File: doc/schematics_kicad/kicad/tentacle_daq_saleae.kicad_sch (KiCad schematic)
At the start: 5 parts, among them T901 tentacle, T902 tentacle, T903 tentacle

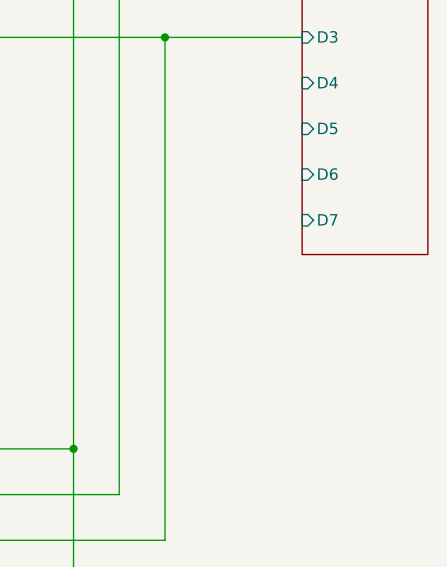
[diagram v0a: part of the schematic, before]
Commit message: MCU names as in micropython-git
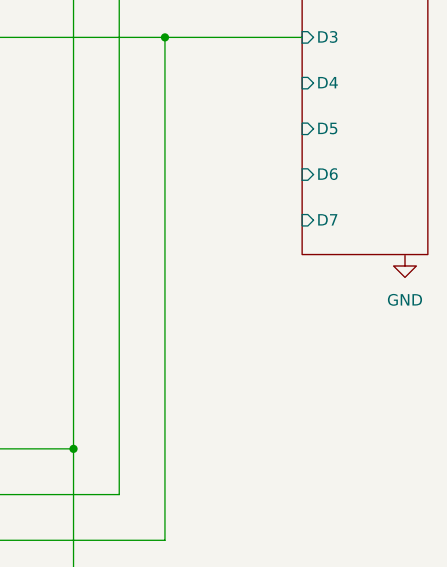
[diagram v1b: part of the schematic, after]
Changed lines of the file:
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@@
+	)
+	(symbol
+		(lib_id "power:GND")
+		(at 194.31 100.33 0)
+		(unit 1)
+		(exclude_from_sim no)
+		(in_bom yes)
+		(on_board yes)
+		(dnp no)
+		(fields_autoplaced yes)
+		(property "Reference" "#PWR0503"
+			(at 194.31 106.68 0)
+			(effects
+				(font
+					(size 1.27 1.27)
+				)
+				(hide yes)
+			)
+		)
+		(property "Value" "GND"
+			(at 194.31 105.41 0)
+			(effects
+				(font
+					(size 1.27 1.27)
+				)
+			)
+		)
+		(property "Footprint" ""
+			(at 194.31 100.33 0)
+			(effects
+				(font
+					(size 1.27 1.27)
+				)
+				(hide yes)
+			)
+		)
+		(property "Datasheet" ""
+			(at 194.31 100.33 0)
+			(effects
+				(font
+					(size 1.27 1.27)
+				)
+				(hide yes)
+			)
+		)
+		(property "Description" "Power symbol creates a global label with name \"GND\" , ground"
+			(at 194.31 100.33 0)
+			(effects
+				(font
+					(size 1.27 1.27)
+				)
+				(hide yes)
+			)
+		)
+		(pin "1"
+		)
+		(instances
+			(project "testbed"
+				(path "/188054c4-74b7-429a-b3f5-c6f3151e27de/2c4ba952-55c5-4e16-806b-8dc205881760"
+					(reference "#PWR0503")
+					(unit 1)
+				)
+			)
+		)
 	)
 	(symbol
